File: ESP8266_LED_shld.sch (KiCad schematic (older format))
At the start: 24 parts, among them J1 Pwr_Dat_Out, J2 CONN_02X08, J3 CONN_DIN, J4 BARREL_JACK, J5 USB-MICROB, J6 CONN_01X06, M1 LOGIC_LEVEL_CONVERTER, U1 ESP-07v2, U2 AMS1117

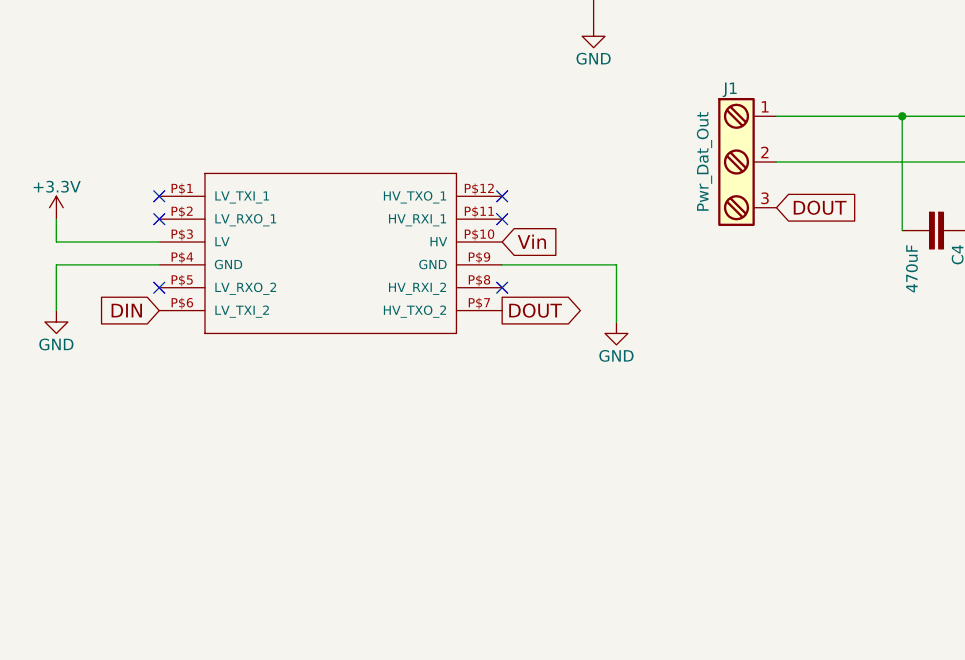
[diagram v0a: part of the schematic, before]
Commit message: added resistor between DOUT and HV4 to protect data pin of LED stip and fixed some silk screen labels (positions)
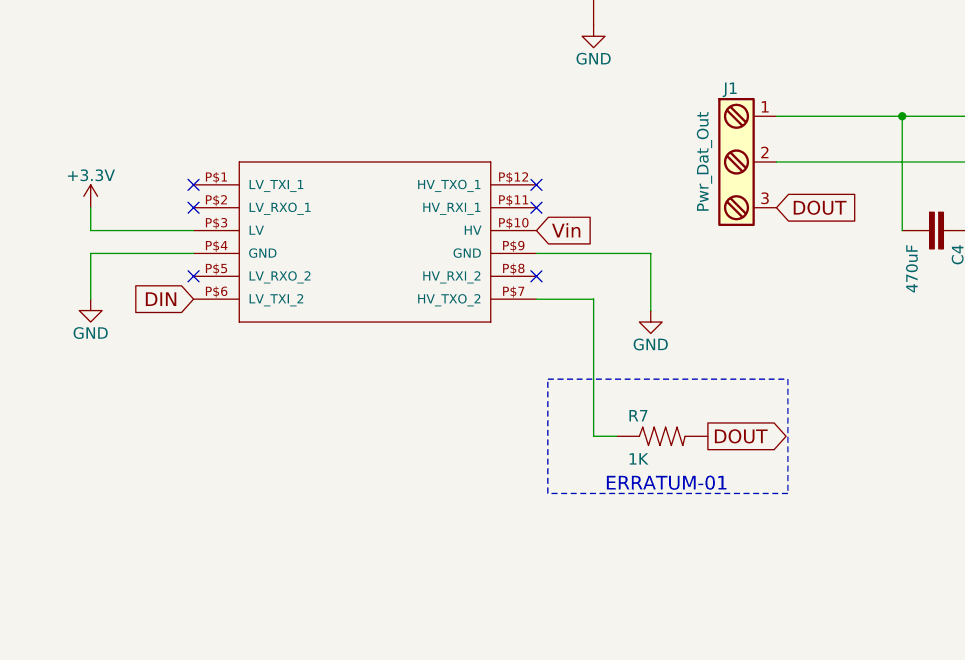
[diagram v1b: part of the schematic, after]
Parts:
- added R7: 1K, Resistors_SMD:R_1206_HandSoldering, symbol RESISTOR1206
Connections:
- net DOUT: now also R7.2; no longer M1.P$7 (HV_TXO_2)
- new net: M1.P$7 (HV_TXO_2), R7.1
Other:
- note added: "ERRATUM-01"
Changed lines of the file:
@@
 L LOGIC_LEVEL_CONVERTER M1
 U 1 1 58DD5864
-P 2600 4800
-F 0 "M1" H 2600 4800 50  0001 C CNN
-F 1 "LOGIC_LEVEL_CONVERTER" H 2600 4800 50  0001 C CNN
-F 2 "SparkFun-Boards:LOGIC_LEVEL_CONVERTER" H 2630 4950 20  0001 C CNN
-F 3 "" H 2600 4800 60  0001 C CNN
-	1    2600 4800
+P 2750 4750
+F 0 "M1" H 2750 4750 50  0001 C CNN
+F 1 "LOGIC_LEVEL_CONVERTER" H 2750 4750 50  0001 C CNN
+F 2 "SparkFun-Boards:LOGIC_LEVEL_CONVERTER" H 2780 4900 20  0001 C CNN
+F 3 "" H 2750 4750 60  0001 C CNN
+	1    2750 4750
 	1    0    0    -1
 $EndComp
@@
 NoConn ~ 10100 3300
 NoConn ~ 10100 3400
-Text GLabel 2900 3800 2    60   Input ~ 0
+Text GLabel 3050 3750 2    60   Input ~ 0
 Vin
 Text GLabel 7250 1600 0    60   Output ~ 0
@@
 Text GLabel 7250 1700 0    60   Output ~ 0
 DIN
-Text GLabel 1400 4100 0    60   Input ~ 0
+Text GLabel 1550 4050 0    60   Input ~ 0
 DIN
-Text GLabel 2900 4100 2    60   Output ~ 0
+Text GLabel 3800 4650 2    60   Output ~ 0
 DOUT
 Text GLabel 4100 3650 2    60   Input ~ 0
@@
 Text GLabel 6550 3350 0    60   Input ~ 0
 GPIO13
-NoConn ~ 2900 3600
-NoConn ~ 2900 3700
-NoConn ~ 2900 4000
-NoConn ~ 1400 4000
-NoConn ~ 1400 3700
-NoConn ~ 1400 3600
+NoConn ~ 3050 3550
+NoConn ~ 3050 3650
+NoConn ~ 3050 3950
+NoConn ~ 1550 3950
+NoConn ~ 1550 3650
+NoConn ~ 1550 3550
 Wire Wire Line
 	9950 1250 10550 1250
@@
 $EndComp
 Wire Wire Line
-	1400 3900 950  3900
-Wire Wire Line
-	950  3900 950  4100
+	1550 3850 1100 3850
+Wire Wire Line
+	1100 3850 1100 4050
 $Comp
 L GND #PWR09
 U 1 1 58DDB559
-P 950 4100
-F 0 "#PWR09" H 950 3850 50  0001 C CNN
-F 1 "GND" H 950 3950 50  0000 C CNN
-F 2 "" H 950 4100 50  0001 C CNN
-F 3 "" H 950 4100 50  0001 C CNN
-	1    950  4100
-	1    0    0    -1
-$EndComp
-Wire Wire Line
-	2900 3900 3400 3900
-Wire Wire Line
-	3400 3900 3400 4150
+P 1100 4050
+F 0 "#PWR09" H 1100 3800 50  0001 C CNN
+F 1 "GND" H 1100 3900 50  0000 C CNN
+F 2 "" H 1100 4050 50  0001 C CNN
+F 3 "" H 1100 4050 50  0001 C CNN
+	1    1100 4050
+	1    0    0    -1
+$EndComp
+Wire Wire Line
+	3050 3850 3550 3850
+Wire Wire Line
+	3550 3850 3550 4100
 $Comp
 L GND #PWR010
 U 1 1 58DDBA94
-P 3400 4150
-F 0 "#PWR010" H 3400 3900 50  0001 C CNN
-F 1 "GND" H 3400 4000 50  0000 C CNN
-F 2 "" H 3400 4150 50  0001 C CNN
-F 3 "" H 3400 4150 50  0001 C CNN
-	1    3400 4150
+P 3550 4100
+F 0 "#PWR010" H 3550 3850 50  0001 C CNN
+F 1 "GND" H 3550 3950 50  0000 C CNN
+F 2 "" H 3550 4100 50  0001 C CNN
+F 3 "" H 3550 4100 50  0001 C CNN
+	1    3550 4100
 	1    0    0    -1
 $EndComp
@@
 $EndComp
 Wire Wire Line
-	1400 3800 950  3800
-Wire Wire Line
-	950  3800 950  3700
+	1550 3750 1100 3750
+Wire Wire Line
+	1100 3750 1100 3650
 $Comp
 L +3.3V #PWR022
 U 1 1 58DFE499
-P 950 3700
-F 0 "#PWR022" H 950 3550 50  0001 C CNN
-F 1 "+3.3V" H 950 3840 50  0000 C CNN
-F 2 "" H 950 3700 50  0001 C CNN
-F 3 "" H 950 3700 50  0001 C CNN
-	1    950  3700
+P 1100 3650
+F 0 "#PWR022" H 1100 3500 50  0001 C CNN
+F 1 "+3.3V" H 1100 3790 50  0000 C CNN
+F 2 "" H 1100 3650 50  0001 C CNN
+F 3 "" H 1100 3650 50  0001 C CNN
+	1    1100 3650
 	1    0    0    -1
 $EndComp
@@
 Text Notes 7750 4000 0    60   ~ 0
 Deep Sleep Wake Up
+$Comp
+L RESISTOR1206 R7
+U 1 1 58E53DEC
+P 3600 4650
+F 0 "R7" H 3450 4709 50  0000 L BNN
+F 1 "1K" H 3450 4520 50  0000 L BNN
+F 2 "Resistors_SMD:R_1206_HandSoldering" H 3630 4800 20  0001 C CNN
+F 3 "" H 3600 4650 60  0001 C CNN
+	1    3600 4650
+	1    0    0    -1
+$EndComp
+Wire Wire Line
+	3300 4650 3400 4650
+Wire Notes Line
+	3100 4400 4150 4400
+Wire Notes Line
+	4150 4400 4150 4900
+Wire Notes Line
+	4150 4900 3100 4900
+Wire Notes Line
+	3100 4900 3100 4400
+Text Notes 3350 4900 0    60   ~ 0
+ERRATUM-01
+Wire Wire Line
+	3050 4050 3300 4050
+Wire Wire Line
+	3300 4050 3300 4650
 $EndSCHEMATC

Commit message: work started on rev2 [wip]
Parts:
- removed M1: LOGIC_LEVEL_CONVERTER, SparkFun-Boards:LOGIC_LEVEL_CONVERTER, symbol LOGIC_LEVEL_CONVERTER
- added Q1, Q2: BSS138, TO_SOT_Packages_SMD:SOT-23, symbol BSS138
- added R10, R8, R9: 10K, Resistors_SMD:R_1206_HandSoldering, symbol RESISTOR1206
- C1, C2: footprint SparkFun-Capacitors:1206 -> Capacitors_SMD:C_1206_HandSoldering
- C3: value 220uF -> 470uF; footprint SparkFun-Capacitors:1206 -> Capacitors_SMD:CP_Elec_8x10; symbol CAP1206 -> CP1
- C4: symbol CAP1206 -> CP1
- J1: footprint Connectors_Terminal_Blocks:TerminalBlock_Pheonix_PT-3.5mm_3pol -> Connectors_Terminal_Blocks:TerminalBlock_Pheonix_MKDS1.5-3pol
- J4: footprint Connectors:BARREL_JACK -> FixedComponents:BARREL_JACK-revision2
- LED1: footprint LEDs:LED_1206 -> FixedComponents:LED_1206-revision2
- R6: value 65 -> 470
- R7: value 1K -> 10K
- U2: footprint SparkFun-PowerIC:V-REG_DPACK-revision2 -> TO_SOT_Packages_SMD:SOT-223-3Lead_TabPin2
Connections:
- net +3V3: now also J2.16 (P16), R7.1, Q1.1 (G), Q2.1 (G), R8.1; no longer J2.10 (P10)
- net ADC: now also J2.10 (P10); no longer J2.16 (P16)
- net CH_PD: now also J2.11 (P11); no longer J2.13 (P13)
- net GND: now also J2.2 (P2); no longer J2.8 (P8)
- net GPIO0: now also J2.3 (P3); no longer J2.5 (P5)
- net GPIO12: now also J2.14 (P14); no longer J2.12 (P12)
- net GPIO13: now also J2.15 (P15); no longer J2.9 (P9)
- net GPIO14: now also J2.13 (P13); no longer J2.11 (P11)
- net GPIO15: now also J2.1 (P1); no longer J2.7 (P7)
- net GPIO16: now also J2.12 (P12); no longer J2.14 (P14)
- net GPIO2: now also J2.4 (P4); no longer J2.6 (P6)
- net GPIO4: now also J2.6 (P6); no longer J2.4 (P4)
- net GPIO5: now also J2.5 (P5); no longer J2.3 (P3)
- net REST: now also J2.9 (P9); no longer J2.15 (P15)
- net RXD: now also J2.8 (P8); no longer J2.2 (P2)
- net TXD: now also J2.7 (P7); no longer J2.1 (P1)
- net DIN renamed LV1
- net LV1: now also Q1.2 (S), R8.2; no longer J3.2 (P2)
- net DOUT renamed HV1
- net HV1: now also Q1.3 (D), R9.2; no longer R7.2
- net Vin renamed VCC
- net VCC: now also R10.1, R9.1
- new net HV2: Q2.3 (D), R10.2
- new net LV2: J3.2 (P2), Q2.2 (S), R7.2
- no-connect marks 10 -> 4
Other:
- note removed: "ERRATUM-01"

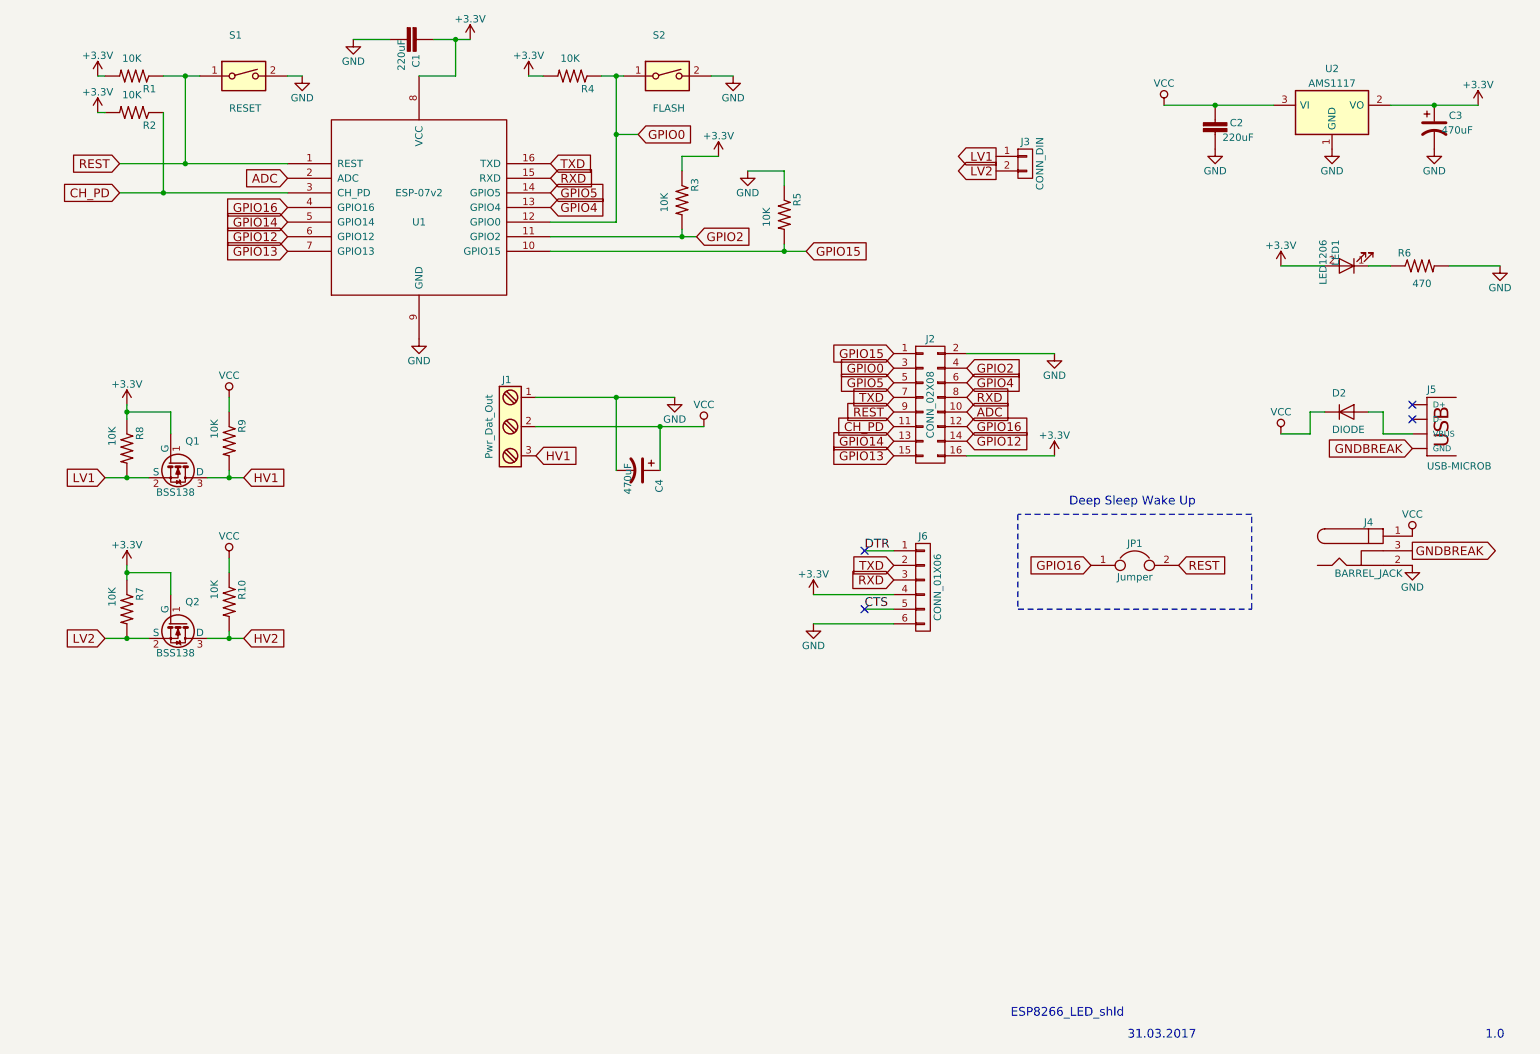
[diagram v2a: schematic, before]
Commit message: changed usb micro b to usb mini b & added CH340G IC. some changes to PCB.
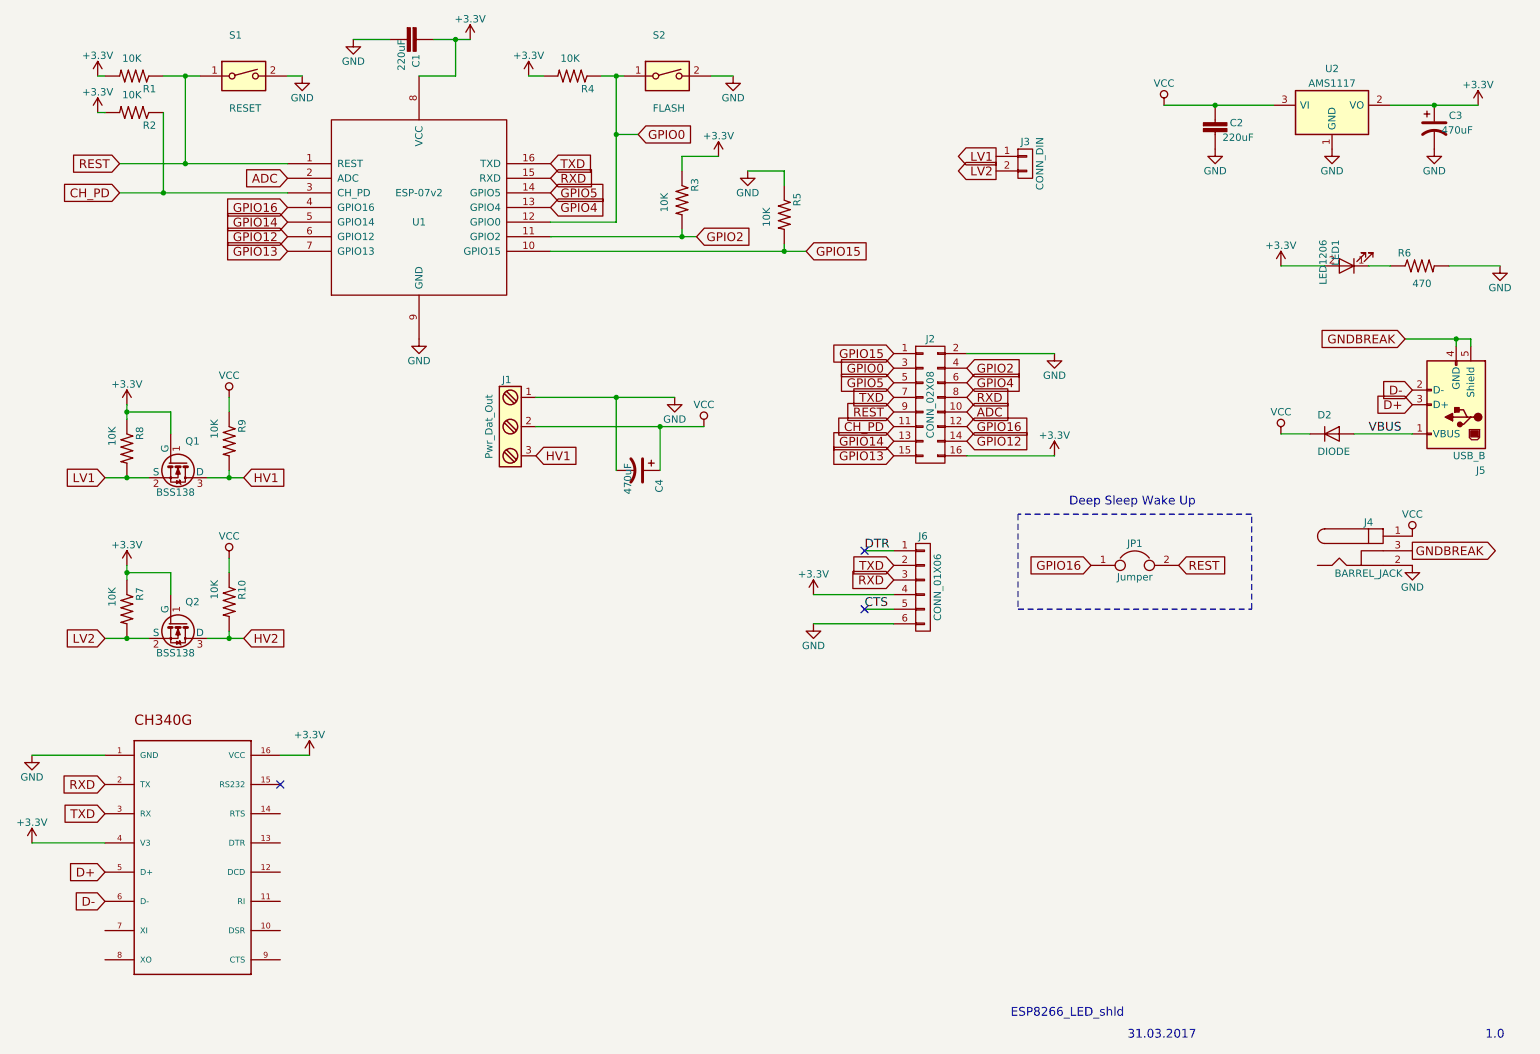
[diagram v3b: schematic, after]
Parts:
- removed J5: USB-MICROB, FixedComponents:USB_Micro-B-revision2, symbol USB-MICROB
- added J5: USB_B, Connectors:USB_Mini-B, symbol USB_B
- added U?: CH340G, SOP-16, symbol CH340G
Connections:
- net +3V3: now also U?.16 (VCC), U?.4 (V3)
- net GND: now also U?.1 (GND)
- net GNDBREAK: now also J5.4 (GND), J5.5 (Shield)
- net RXD: now also U?.2 (TX)
- net TXD: now also U?.3 (RX)
- net VBUS: now reaches D2.2 (A)
- net VBUS: now also J5.1 (VBUS)
- new net D+: J5.3 (D+), U?.5 (D+)
- new net D-: J5.2 (D-), U?.6 (D-)
- no-connect marks 4 -> 3
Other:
- moved on the sheet: D2
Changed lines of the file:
@@
 LIBS:contrib
 LIBS:valves
+LIBS:CH340G
 LIBS:ESP8266
 LIBS:adafruit
@@
 $EndComp
 $Comp
-L USB-MICROB J5
-U 1 1 58DD5E02
-P 10200 3600
-F 0 "J5" H 10200 3975 50  0000 L BNN
-F 1 "USB-MICROB" H 10200 3450 50  0000 L BNN
-F 2 "FixedComponents:USB_Micro-B-revision2" H 10230 3750 20  0001 C CNN
-F 3 "" H 10200 3600 60  0000 C CNN
-	1    10200 3600
-	1    0    0    -1
-$EndComp
-$Comp
 L BARREL_JACK J4
 U 1 1 58DD5E5D
@@
 L D D2
 U 1 1 58DD5FC4
-P 9650 3350
-F 0 "D2" H 9550 3450 50  0000 L BNN
-F 1 "DIODE" H 9550 3200 50  0000 L BNN
-F 2 "Diodes_SMD:D_SOD-323_HandSoldering" H 9680 3500 20  0001 C CNN
-F 3 "" H 9650 3350 60  0001 C CNN
-	1    9650 3350
+P 9550 3500
+F 0 "D2" H 9450 3600 50  0000 L BNN
+F 1 "DIODE" H 9450 3350 50  0000 L BNN
+F 2 "Diodes_SMD:D_SOD-323_HandSoldering" H 9580 3650 20  0001 C CNN
+F 3 "" H 9550 3500 60  0001 C CNN
+	1    9550 3500
 	1    0    0    -1
 $EndComp
@@
 Text GLabel 10100 4300 2    60   Output ~ 0
 GNDBREAK
-NoConn ~ 10100 3300
-NoConn ~ 10100 3400
 Text GLabel 7250 1600 0    60   Output ~ 0
 LV1
@@
 $EndComp
 Wire Wire Line
-	10100 3500 9900 3500
-Wire Wire Line
-	9900 3500 9900 3350
-Wire Wire Line
-	9900 3350 9800 3350
-Wire Wire Line
-	9500 3350 9400 3350
-Wire Wire Line
-	9400 3350 9400 3500
-Wire Wire Line
-	9400 3500 9200 3500
+	9700 3500 10100 3500
+Wire Wire Line
+	9200 3500 9400 3500
 $Comp
 L RESISTOR1206 R3
@@
 Wire Wire Line
 	2400 1050 2500 1050
-Text GLabel 10100 3600 0    60   Input ~ 0
+Text GLabel 10050 2850 0    60   Input ~ 0
 GNDBREAK
 $Comp
@@
 	1    0    0    -1
 $EndComp
+$Comp
+L USB_B J5
+U 1 1 58F90BD6
+P 10400 3300
+F 0 "J5" H 10200 3750 50  0000 L CNN
+F 1 "USB_B" H 10200 3650 50  0000 L CNN
+F 2 "Connectors:USB_Mini-B" H 10550 3250 50  0001 C CNN
+F 3 "" H 10550 3250 50  0001 C CNN
+	1    10400 3300
+	-1   0    0    1
+$EndComp
+Wire Wire Line
+	10050 2850 10500 2850
+Text Label 9800 3500 0    60   ~ 0
+VBUS
+Wire Wire Line
+	10400 2850 10400 2900
+Wire Wire Line
+	10500 2850 10500 2900
+Connection ~ 10400 2850
+$Comp
+L CH340G U?
+U 1 1 58F91D58
+P 1750 6400
+F 0 "U?" H 1750 6400 50  0001 L CNN
+F 1 "CH340G" H 1750 6400 50  0001 L CNN
+F 2 "SOP-16" H 1750 6400 50  0001 L CNN
+F 3 "" H 1750 6400 60  0001 C CNN
+	1    1750 6400
+	1    0    0    -1
+$EndComp
+$Comp
+L GND #PWR?
+U 1 1 58F9490C
+P 650 5700
+F 0 "#PWR?" H 650 5450 50  0001 C CNN
+F 1 "GND" H 650 5550 50  0000 C CNN
+F 2 "" H 650 5700 50  0001 C CNN
+F 3 "" H 650 5700 50  0001 C CNN
+	1    650  5700
+	1    0    0    -1
+$EndComp
+Wire Wire Line
+	1150 5700 650  5700
+$Comp
+L +3.3V #PWR?
+U 1 1 58F957B2
+P 2550 5700
+F 0 "#PWR?" H 2550 5550 50  0001 C CNN
+F 1 "+3.3V" H 2550 5840 50  0000 C CNN
+F 2 "" H 2550 5700 50  0001 C CNN
+F 3 "" H 2550 5700 50  0001 C CNN
+	1    2550 5700
+	1    0    0    -1
+$EndComp
+Wire Wire Line
+	2350 5700 2550 5700
+$Comp
+L +3.3V #PWR?
+U 1 1 58F95A00
+P 650 6300
+F 0 "#PWR?" H 650 6150 50  0001 C CNN
+F 1 "+3.3V" H 650 6440 50  0000 C CNN
+F 2 "" H 650 6300 50  0001 C CNN
+F 3 "" H 650 6300 50  0001 C CNN
+	1    650  6300
+	1    0    0    -1
+$EndComp
+Wire Wire Line
+	1150 6300 650  6300
+NoConn ~ 2350 5900
+Text GLabel 1150 5900 0    60   Input ~ 0
+RXD
+Text GLabel 1150 6100 0    60   Input ~ 0
+TXD
+Text GLabel 10100 3200 0    60   Input ~ 0
+D-
+Text GLabel 10100 3300 0    60   Input ~ 0
+D+
+Text GLabel 1150 6700 0    60   Input ~ 0
+D-
+Text GLabel 1150 6500 0    60   Input ~ 0
+D+
 $EndSCHEMATC
